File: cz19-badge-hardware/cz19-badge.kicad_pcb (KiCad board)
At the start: 2 copper layers, 128 parts

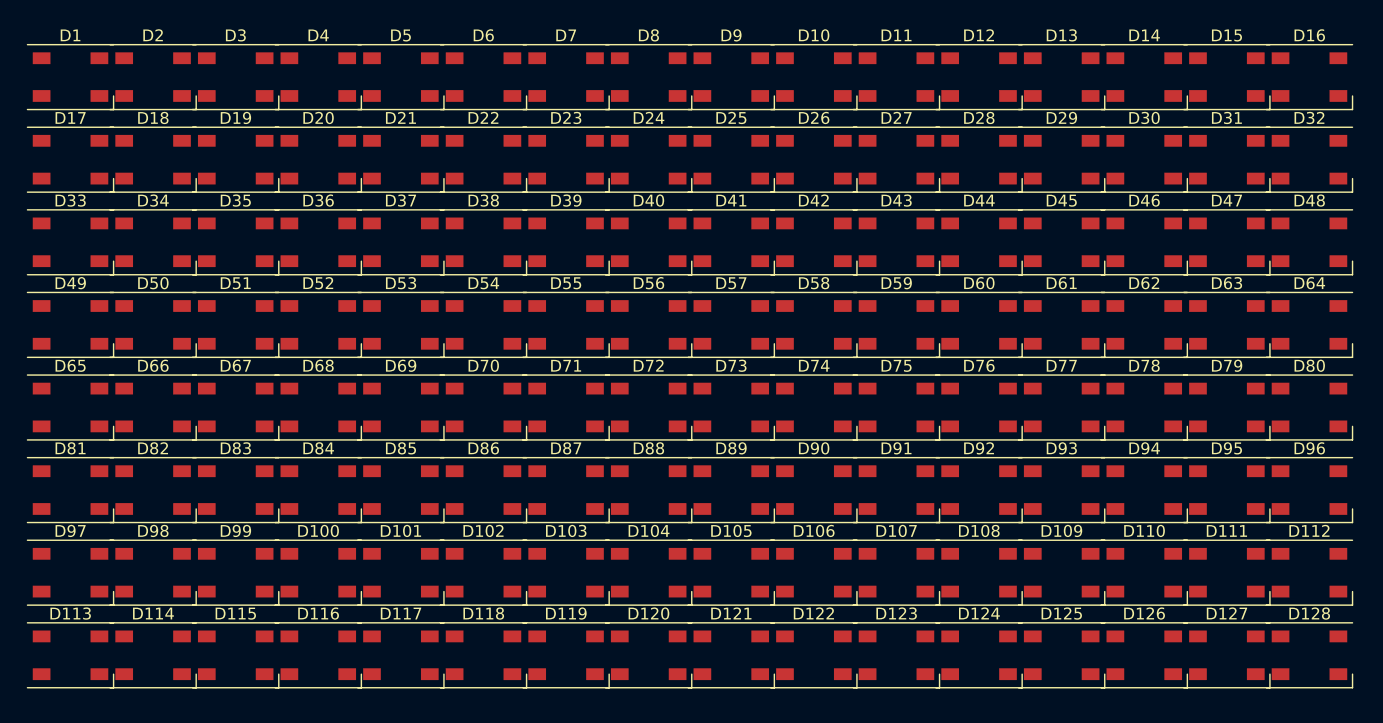
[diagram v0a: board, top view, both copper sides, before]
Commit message: Finished components for USB flashing, and controlling the LEDs w/ mosfet power
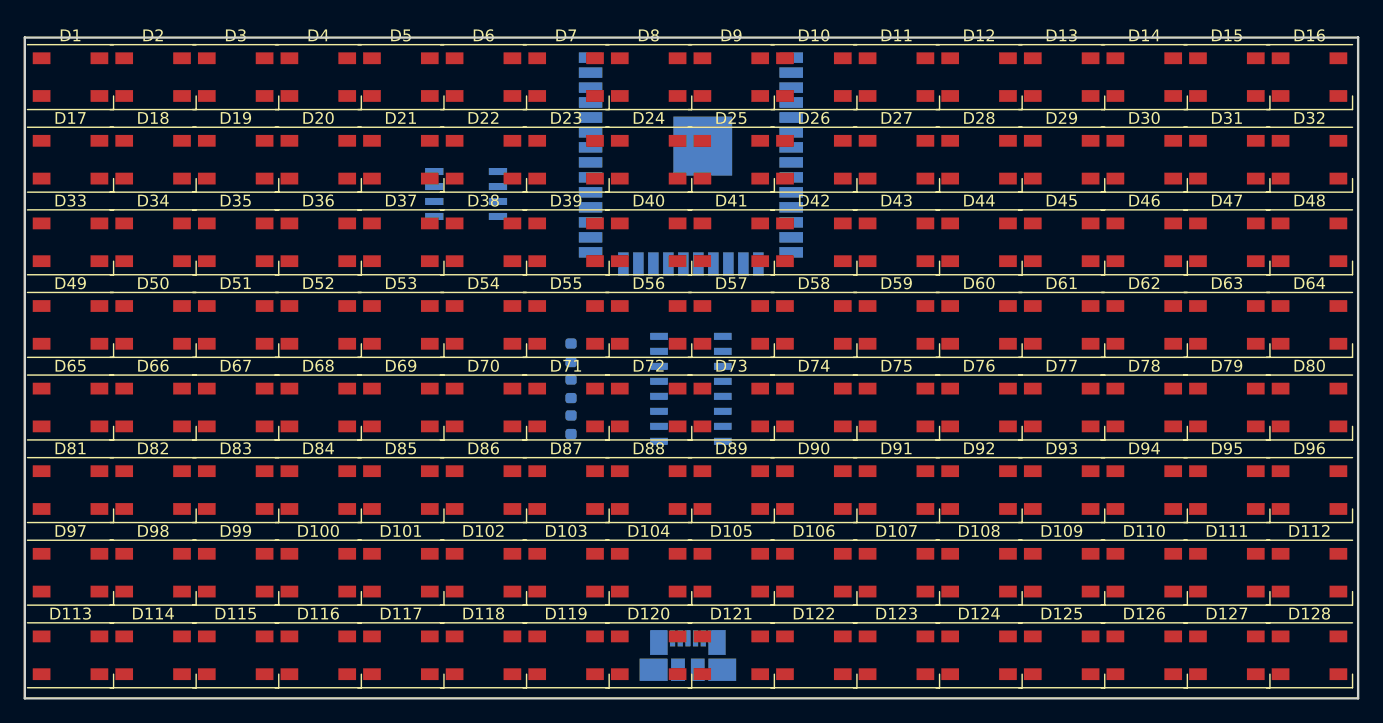
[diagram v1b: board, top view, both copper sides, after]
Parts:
- added J1: USB_B_Micro, Connector_USB:USB_Micro-B_Molex_47346-0001, B.Cu at (76.2, 71.4)
- added Q1: FDS8896, Package_SO:SOIC-8_3.9x4.9mm_P1.27mm, B.Cu at (57.4, 32.3)
- added R1: 10k, Resistor_SMD:R_0603_1608Metric, B.Cu at (66.3, 51.8)
- added R2: 10k, Resistor_SMD:R_0603_1608Metric, B.Cu at (66.3, 48.8)
- added R3: 10k, Resistor_SMD:R_0603_1608Metric, B.Cu at (66.3, 45.7)
- added U1: CH340C, Package_SO:SOIC-16_3.9x9.9mm_P1.27mm, B.Cu at (76.5, 48.8)
- added U2: ESP32-WROOM-32D, RF_Module:ESP32-WROOM-32, B.Cu at (76.5, 28.9)
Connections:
- net /LEDs/LEDS_OUT renamed LEDS_OUT
- net 3V3 renamed VCC
- D1 pad 2: /LEDs/LEDS_IN -> LEDS_IN
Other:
- board outline added: 113 x 56 mm
- copper layers 2 -> 4

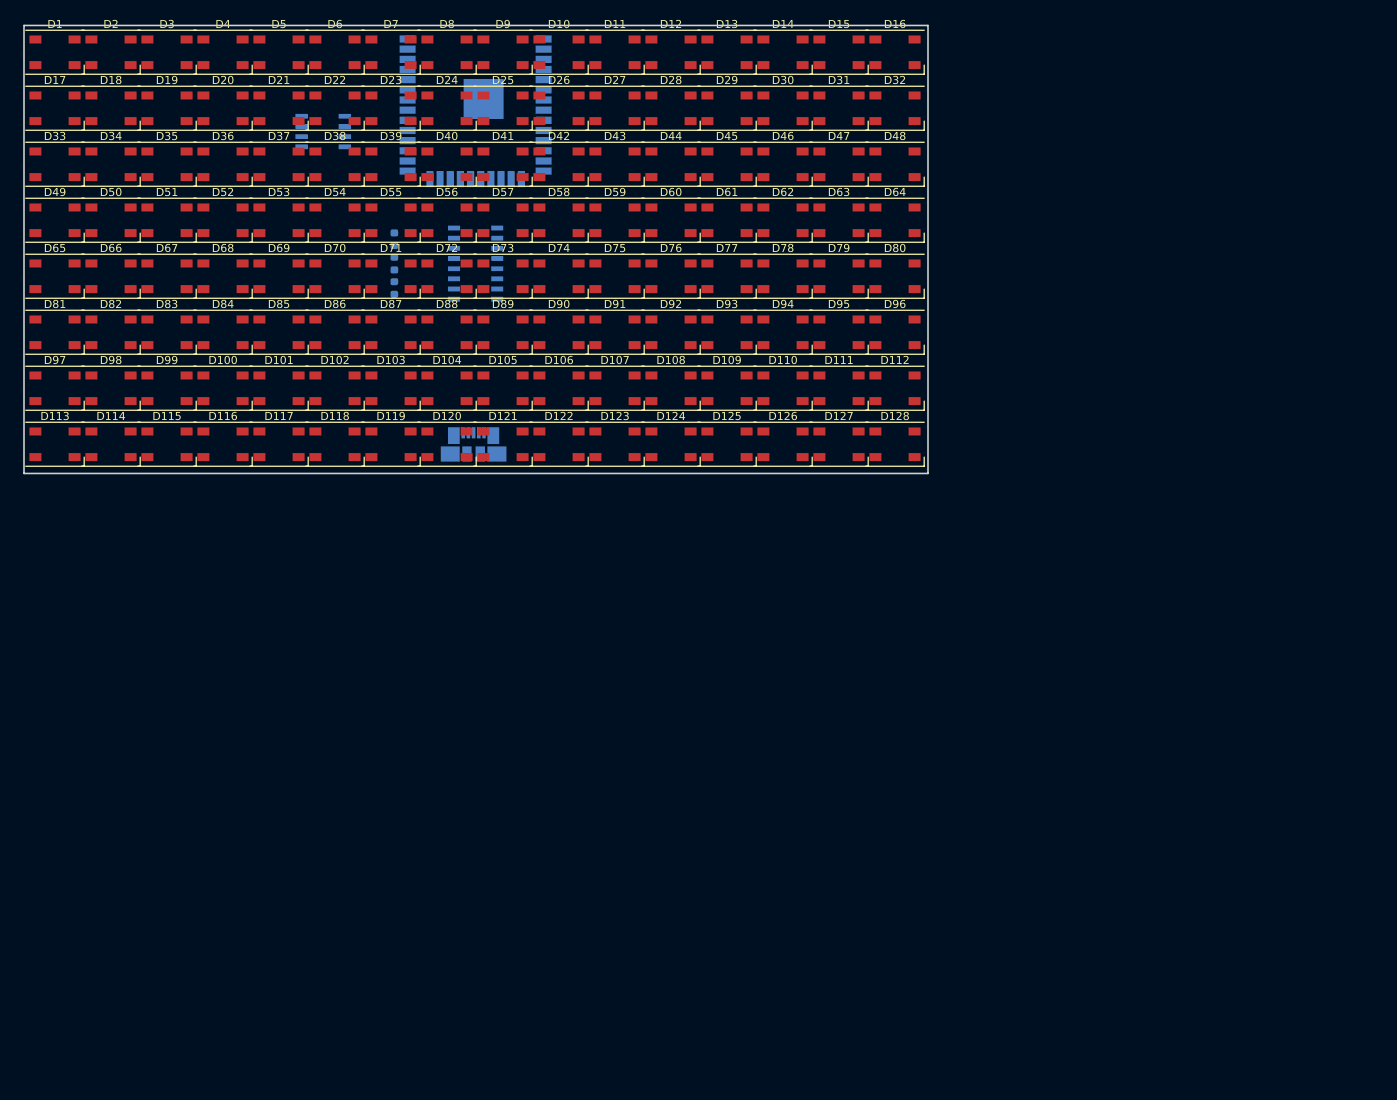
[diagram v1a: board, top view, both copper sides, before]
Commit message: Added extra led columns w/ solder jumper to go back to 8x16, added RTS/DTR fets instead of diodes, added battery circuit w/ reverse polarity protection + automatic switching to USB power
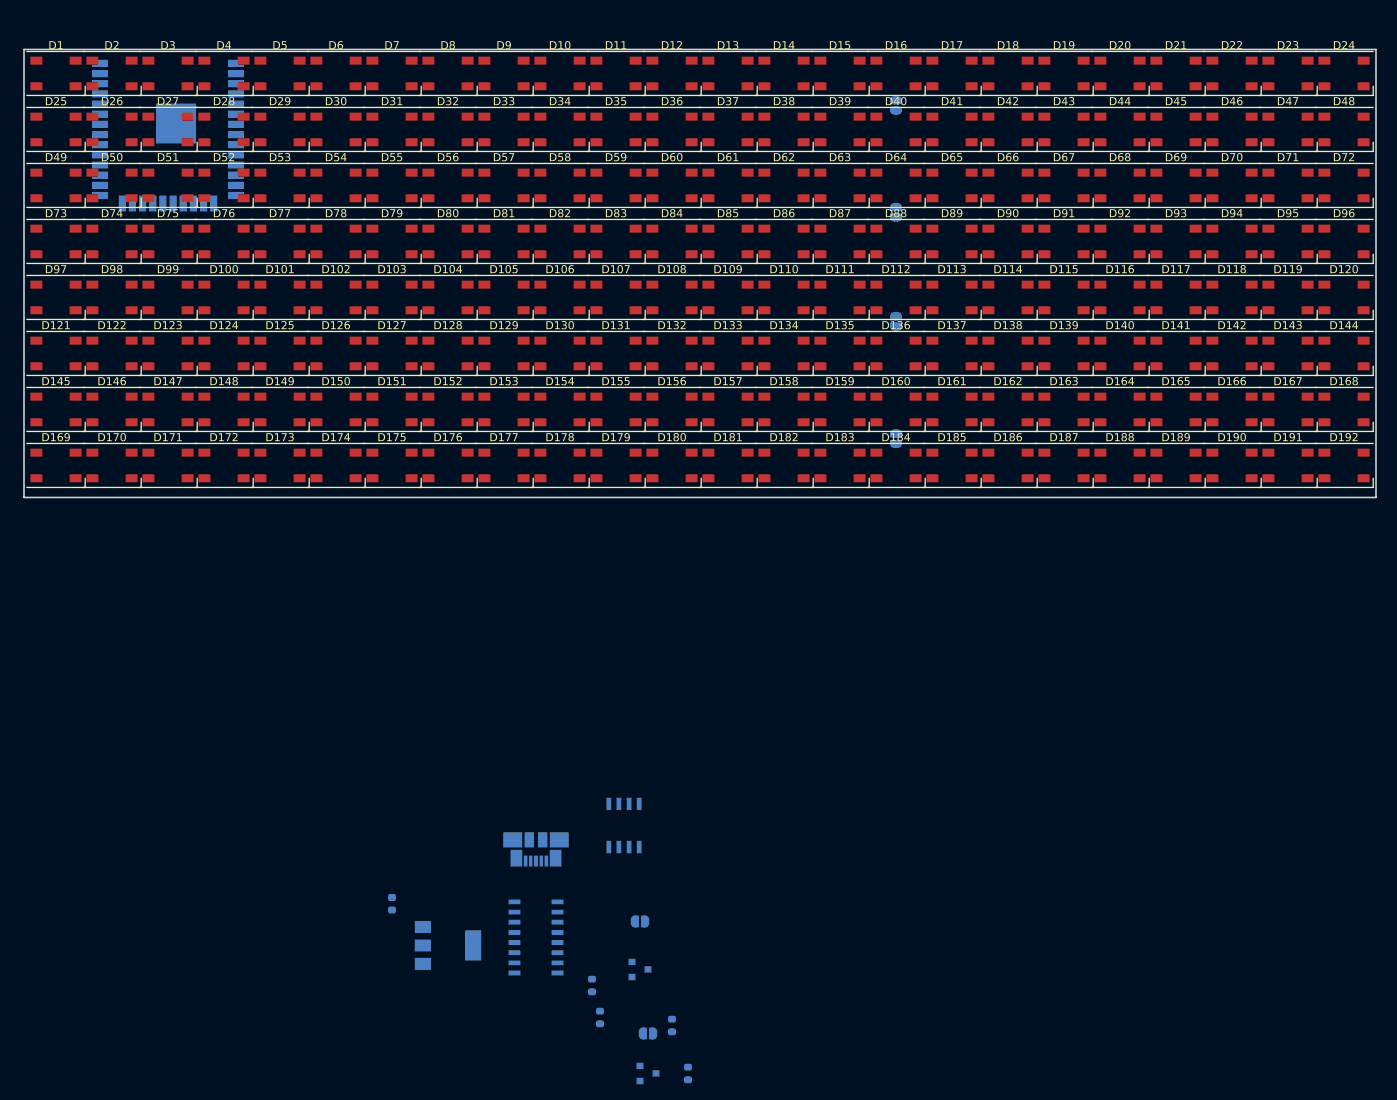
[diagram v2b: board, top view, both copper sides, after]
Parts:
- added D129: SK6812, LED_SMD:LED_SK6812_PLCC4_5.0x5.0mm_P3.2mm, F.Cu at (80.0, 60.0)
- added D130: SK6812, LED_SMD:LED_SK6812_PLCC4_5.0x5.0mm_P3.2mm, F.Cu at (87.0, 60.0)
- added D131: SK6812, LED_SMD:LED_SK6812_PLCC4_5.0x5.0mm_P3.2mm, F.Cu at (94.0, 60.0)
- added D132: SK6812, LED_SMD:LED_SK6812_PLCC4_5.0x5.0mm_P3.2mm, F.Cu at (101.0, 60.0)
- added D133: SK6812, LED_SMD:LED_SK6812_PLCC4_5.0x5.0mm_P3.2mm, F.Cu at (108.0, 60.0)
- added D134: SK6812, LED_SMD:LED_SK6812_PLCC4_5.0x5.0mm_P3.2mm, F.Cu at (115.0, 60.0)
- added D135: SK6812, LED_SMD:LED_SK6812_PLCC4_5.0x5.0mm_P3.2mm, F.Cu at (122.0, 60.0)
- added D136: SK6812, LED_SMD:LED_SK6812_PLCC4_5.0x5.0mm_P3.2mm, F.Cu at (129.0, 60.0)
- added D137: SK6812, LED_SMD:LED_SK6812_PLCC4_5.0x5.0mm_P3.2mm, F.Cu at (136.0, 60.0)
- added D138: SK6812, LED_SMD:LED_SK6812_PLCC4_5.0x5.0mm_P3.2mm, F.Cu at (143.0, 60.0)
- added D139: SK6812, LED_SMD:LED_SK6812_PLCC4_5.0x5.0mm_P3.2mm, F.Cu at (150.0, 60.0)
- added D140: SK6812, LED_SMD:LED_SK6812_PLCC4_5.0x5.0mm_P3.2mm, F.Cu at (157.0, 60.0)
- added D141: SK6812, LED_SMD:LED_SK6812_PLCC4_5.0x5.0mm_P3.2mm, F.Cu at (164.0, 60.0)
- added D142: SK6812, LED_SMD:LED_SK6812_PLCC4_5.0x5.0mm_P3.2mm, F.Cu at (171.0, 60.0)
- added D143: SK6812, LED_SMD:LED_SK6812_PLCC4_5.0x5.0mm_P3.2mm, F.Cu at (178.0, 60.0)
- added D144: SK6812, LED_SMD:LED_SK6812_PLCC4_5.0x5.0mm_P3.2mm, F.Cu at (185.0, 60.0)
- added D145: SK6812, LED_SMD:LED_SK6812_PLCC4_5.0x5.0mm_P3.2mm, F.Cu at (24.0, 67.0)
- added D146: SK6812, LED_SMD:LED_SK6812_PLCC4_5.0x5.0mm_P3.2mm, F.Cu at (31.0, 67.0)
- added D147: SK6812, LED_SMD:LED_SK6812_PLCC4_5.0x5.0mm_P3.2mm, F.Cu at (38.0, 67.0)
- added D148: SK6812, LED_SMD:LED_SK6812_PLCC4_5.0x5.0mm_P3.2mm, F.Cu at (45.0, 67.0)
- added D149: SK6812, LED_SMD:LED_SK6812_PLCC4_5.0x5.0mm_P3.2mm, F.Cu at (52.0, 67.0)
- added D150: SK6812, LED_SMD:LED_SK6812_PLCC4_5.0x5.0mm_P3.2mm, F.Cu at (59.0, 67.0)
- added D151: SK6812, LED_SMD:LED_SK6812_PLCC4_5.0x5.0mm_P3.2mm, F.Cu at (66.0, 67.0)
- added D152: SK6812, LED_SMD:LED_SK6812_PLCC4_5.0x5.0mm_P3.2mm, F.Cu at (73.0, 67.0)
- added D153: SK6812, LED_SMD:LED_SK6812_PLCC4_5.0x5.0mm_P3.2mm, F.Cu at (80.0, 67.0)
- added D154: SK6812, LED_SMD:LED_SK6812_PLCC4_5.0x5.0mm_P3.2mm, F.Cu at (87.0, 67.0)
- added D155: SK6812, LED_SMD:LED_SK6812_PLCC4_5.0x5.0mm_P3.2mm, F.Cu at (94.0, 67.0)
- added D156: SK6812, LED_SMD:LED_SK6812_PLCC4_5.0x5.0mm_P3.2mm, F.Cu at (101.0, 67.0)
- added D157: SK6812, LED_SMD:LED_SK6812_PLCC4_5.0x5.0mm_P3.2mm, F.Cu at (108.0, 67.0)
- added D158: SK6812, LED_SMD:LED_SK6812_PLCC4_5.0x5.0mm_P3.2mm, F.Cu at (115.0, 67.0)
- added D159: SK6812, LED_SMD:LED_SK6812_PLCC4_5.0x5.0mm_P3.2mm, F.Cu at (122.0, 67.0)
- added D160: SK6812, LED_SMD:LED_SK6812_PLCC4_5.0x5.0mm_P3.2mm, F.Cu at (129.0, 67.0)
- added D161: SK6812, LED_SMD:LED_SK6812_PLCC4_5.0x5.0mm_P3.2mm, F.Cu at (136.0, 67.0)
- added D162: SK6812, LED_SMD:LED_SK6812_PLCC4_5.0x5.0mm_P3.2mm, F.Cu at (143.0, 67.0)
- added D163: SK6812, LED_SMD:LED_SK6812_PLCC4_5.0x5.0mm_P3.2mm, F.Cu at (150.0, 67.0)
- added D164: SK6812, LED_SMD:LED_SK6812_PLCC4_5.0x5.0mm_P3.2mm, F.Cu at (157.0, 67.0)
- added D165: SK6812, LED_SMD:LED_SK6812_PLCC4_5.0x5.0mm_P3.2mm, F.Cu at (164.0, 67.0)
- added D166: SK6812, LED_SMD:LED_SK6812_PLCC4_5.0x5.0mm_P3.2mm, F.Cu at (171.0, 67.0)
- added D167: SK6812, LED_SMD:LED_SK6812_PLCC4_5.0x5.0mm_P3.2mm, F.Cu at (178.0, 67.0)
- added D168: SK6812, LED_SMD:LED_SK6812_PLCC4_5.0x5.0mm_P3.2mm, F.Cu at (185.0, 67.0)
- added D169: SK6812, LED_SMD:LED_SK6812_PLCC4_5.0x5.0mm_P3.2mm, F.Cu at (24.0, 74.0)
- added D170: SK6812, LED_SMD:LED_SK6812_PLCC4_5.0x5.0mm_P3.2mm, F.Cu at (31.0, 74.0)
- added D171: SK6812, LED_SMD:LED_SK6812_PLCC4_5.0x5.0mm_P3.2mm, F.Cu at (38.0, 74.0)
- added D172: SK6812, LED_SMD:LED_SK6812_PLCC4_5.0x5.0mm_P3.2mm, F.Cu at (45.0, 74.0)
- added D173: SK6812, LED_SMD:LED_SK6812_PLCC4_5.0x5.0mm_P3.2mm, F.Cu at (52.0, 74.0)
- added D174: SK6812, LED_SMD:LED_SK6812_PLCC4_5.0x5.0mm_P3.2mm, F.Cu at (59.0, 74.0)
- added D175: SK6812, LED_SMD:LED_SK6812_PLCC4_5.0x5.0mm_P3.2mm, F.Cu at (66.0, 74.0)
- added D176: SK6812, LED_SMD:LED_SK6812_PLCC4_5.0x5.0mm_P3.2mm, F.Cu at (73.0, 74.0)
- added D177: SK6812, LED_SMD:LED_SK6812_PLCC4_5.0x5.0mm_P3.2mm, F.Cu at (80.0, 74.0)
- added D178: SK6812, LED_SMD:LED_SK6812_PLCC4_5.0x5.0mm_P3.2mm, F.Cu at (87.0, 74.0)
- added D179: SK6812, LED_SMD:LED_SK6812_PLCC4_5.0x5.0mm_P3.2mm, F.Cu at (94.0, 74.0)
- added D180: SK6812, LED_SMD:LED_SK6812_PLCC4_5.0x5.0mm_P3.2mm, F.Cu at (101.0, 74.0)
- added D181: SK6812, LED_SMD:LED_SK6812_PLCC4_5.0x5.0mm_P3.2mm, F.Cu at (108.0, 74.0)
- added D182: SK6812, LED_SMD:LED_SK6812_PLCC4_5.0x5.0mm_P3.2mm, F.Cu at (115.0, 74.0)
- added D183: SK6812, LED_SMD:LED_SK6812_PLCC4_5.0x5.0mm_P3.2mm, F.Cu at (122.0, 74.0)
- added D184: SK6812, LED_SMD:LED_SK6812_PLCC4_5.0x5.0mm_P3.2mm, F.Cu at (129.0, 74.0)
- added D185: SK6812, LED_SMD:LED_SK6812_PLCC4_5.0x5.0mm_P3.2mm, F.Cu at (136.0, 74.0)
- added D186: SK6812, LED_SMD:LED_SK6812_PLCC4_5.0x5.0mm_P3.2mm, F.Cu at (143.0, 74.0)
- added D187: SK6812, LED_SMD:LED_SK6812_PLCC4_5.0x5.0mm_P3.2mm, F.Cu at (150.0, 74.0)
- added D188: SK6812, LED_SMD:LED_SK6812_PLCC4_5.0x5.0mm_P3.2mm, F.Cu at (157.0, 74.0)
- added D189: SK6812, LED_SMD:LED_SK6812_PLCC4_5.0x5.0mm_P3.2mm, F.Cu at (164.0, 74.0)
- added D190: SK6812, LED_SMD:LED_SK6812_PLCC4_5.0x5.0mm_P3.2mm, F.Cu at (171.0, 74.0)
- added D191: SK6812, LED_SMD:LED_SK6812_PLCC4_5.0x5.0mm_P3.2mm, F.Cu at (178.0, 74.0)
- added D192: SK6812, LED_SMD:LED_SK6812_PLCC4_5.0x5.0mm_P3.2mm, F.Cu at (185.0, 74.0)
- added JP1: SolderJumper_2_Open, Jumper:SolderJumper-2_P1.3mm_Open_RoundedPad1.0x1.5mm, B.Cu at (97.0, 131.0)
- added JP2: SolderJumper_2_Open, Jumper:SolderJumper-2_P1.3mm_Open_RoundedPad1.0x1.5mm, B.Cu at (98.0, 145.0)
- added JP3: SolderJumper_2_Open, Jumper:SolderJumper-2_P1.3mm_Open_RoundedPad1.0x1.5mm, B.Cu at (129.0, 29.0)
- added JP4: SolderJumper_2_Open, Jumper:SolderJumper-2_P1.3mm_Open_RoundedPad1.0x1.5mm, B.Cu at (129.0, 42.4)
- added JP5: SolderJumper_2_Open, Jumper:SolderJumper-2_P1.3mm_Open_RoundedPad1.0x1.5mm, B.Cu at (129.0, 56.0)
- added JP6: SolderJumper_2_Open, Jumper:SolderJumper-2_P1.3mm_Open_RoundedPad1.0x1.5mm, B.Cu at (129.0, 70.7)
- added Q2: MMBT2222A, Package_TO_SOT_SMD:SOT-23, B.Cu at (98.0, 150.0)
- added Q3: FDS8896, Package_SO:SOIC-8_3.9x4.9mm_P1.27mm, B.Cu at (95.0, 119.0)
- added R4: 10k, Resistor_SMD:R_0603_1608Metric, B.Cu at (66.0, 128.8)
- added R5: 10k, Resistor_SMD:R_0603_1608Metric, B.Cu at (103.0, 150.0)
- added U3: AMS1117, Package_TO_SOT_SMD:SOT-223-3_TabPin2, B.Cu at (73.0, 134.0)
- Q1: value FDS8896 -> MMBT2222A; footprint Package_SO:SOIC-8_3.9x4.9mm_P1.27mm -> Package_TO_SOT_SMD:SOT-23
- moved D113 113.6 mm to (136.0, 53.0)
- moved D114 113.6 mm to (143.0, 53.0)
- moved D115 113.6 mm to (150.0, 53.0)
- moved D116 113.6 mm to (157.0, 53.0)
- moved D117 113.6 mm to (164.0, 53.0)
- moved D118 113.6 mm to (171.0, 53.0)
- moved D119 113.6 mm to (178.0, 53.0)
- moved D120 113.6 mm to (185.0, 53.0)
- moved D65 112.7 mm to (136.0, 39.0)
- moved D66 112.7 mm to (143.0, 39.0)
- moved D67 112.7 mm to (150.0, 39.0)
- moved D68 112.7 mm to (157.0, 39.0)
- moved D69 112.7 mm to (164.0, 39.0)
- moved D70 112.7 mm to (171.0, 39.0)
- moved D71 112.7 mm to (178.0, 39.0)
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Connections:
- D1 pad 1: VCC -> 5V_USB
- D10 pad 1: VCC -> 5V_USB
- D100 pad 1: VCC -> 5V_USB
- D101 pad 1: VCC -> 5V_USB
- D102 pad 1: VCC -> 5V_USB
- D103 pad 1: VCC -> 5V_USB
- D104 pad 1: VCC -> 5V_USB
- D105 pad 1: VCC -> 5V_USB
- D106 pad 1: VCC -> 5V_USB
- D107 pad 1: VCC -> 5V_USB
- D108 pad 1: VCC -> 5V_USB
- D109 pad 1: VCC -> 5V_USB
- D11 pad 1: VCC -> 5V_USB
- D110 pad 1: VCC -> 5V_USB
- D111 pad 1: VCC -> 5V_USB
- D112 pad 1: VCC -> 5V_USB
- D113 pad 1: VCC -> 5V_USB
- D113 pad 2: Net-(D113-Pad2) -> Net-(D112-Pad4)
- D113 pad 4: LEDS_OUT -> Net-(D113-Pad4)
- D114 pad 1: VCC -> 5V_USB
- D114 pad 2: Net-(D114-Pad2) -> Net-(D113-Pad4)
- D114 pad 4: Net-(D113-Pad2) -> Net-(D114-Pad4)
- D115 pad 1: VCC -> 5V_USB
- D115 pad 2: Net-(D115-Pad2) -> Net-(D114-Pad4)
- D115 pad 4: Net-(D114-Pad2) -> Net-(D115-Pad4)
- D116 pad 1: VCC -> 5V_USB
- D116 pad 2: Net-(D116-Pad2) -> Net-(D115-Pad4)
- D116 pad 4: Net-(D115-Pad2) -> Net-(D116-Pad4)
- D117 pad 1: VCC -> 5V_USB
- D117 pad 2: Net-(D117-Pad2) -> Net-(D116-Pad4)
- D117 pad 4: Net-(D116-Pad2) -> Net-(D117-Pad4)
- D118 pad 1: VCC -> 5V_USB
- D118 pad 2: Net-(D118-Pad2) -> Net-(D117-Pad4)
- D118 pad 4: Net-(D117-Pad2) -> Net-(D118-Pad4)
- D119 pad 1: VCC -> 5V_USB
- D119 pad 2: Net-(D119-Pad2) -> Net-(D118-Pad4)
- D119 pad 4: Net-(D118-Pad2) -> Net-(D119-Pad4)
- D12 pad 1: VCC -> 5V_USB
- D120 pad 1: VCC -> 5V_USB
- D120 pad 2: Net-(D120-Pad2) -> Net-(D119-Pad4)
- D120 pad 4: Net-(D119-Pad2) -> Net-(D120-Pad4)
- D121 pad 1: VCC -> 5V_USB
- D121 pad 4: Net-(D120-Pad2) -> Net-(D121-Pad4)
- D122 pad 1: VCC -> 5V_USB
- D123 pad 1: VCC -> 5V_USB
- D124 pad 1: VCC -> 5V_USB
- D125 pad 1: VCC -> 5V_USB
- D126 pad 1: VCC -> 5V_USB
- D127 pad 1: VCC -> 5V_USB
- D128 pad 1: VCC -> 5V_USB
- D128 pad 2: Net-(D112-Pad4) -> Net-(D128-Pad2)
- D13 pad 1: VCC -> 5V_USB
- D14 pad 1: VCC -> 5V_USB
- D15 pad 1: VCC -> 5V_USB
- D16 pad 1: VCC -> 5V_USB
- D17 pad 1: VCC -> 5V_USB
- D17 pad 2: Net-(D17-Pad2) -> Net-(D16-Pad4)
- D18 pad 1: VCC -> 5V_USB
- D18 pad 2: Net-(D18-Pad2) -> Net-(D17-Pad4)
- D18 pad 4: Net-(D17-Pad2) -> Net-(D18-Pad4)
- D19 pad 1: VCC -> 5V_USB
- D19 pad 2: Net-(D19-Pad2) -> Net-(D18-Pad4)
- D19 pad 4: Net-(D18-Pad2) -> Net-(D19-Pad4)
- D2 pad 1: VCC -> 5V_USB
- D20 pad 1: VCC -> 5V_USB
- D20 pad 2: Net-(D20-Pad2) -> Net-(D19-Pad4)
- D20 pad 4: Net-(D19-Pad2) -> Net-(D20-Pad4)
- D21 pad 1: VCC -> 5V_USB
- D21 pad 2: Net-(D21-Pad2) -> Net-(D20-Pad4)
- D21 pad 4: Net-(D20-Pad2) -> Net-(D21-Pad4)
- D22 pad 1: VCC -> 5V_USB
- D22 pad 2: Net-(D22-Pad2) -> Net-(D21-Pad4)
- D22 pad 4: Net-(D21-Pad2) -> Net-(D22-Pad4)
- D23 pad 1: VCC -> 5V_USB
- D23 pad 2: Net-(D23-Pad2) -> Net-(D22-Pad4)
- D23 pad 4: Net-(D22-Pad2) -> Net-(D23-Pad4)
- D24 pad 1: VCC -> 5V_USB
- D24 pad 2: Net-(D24-Pad2) -> Net-(D23-Pad4)
- D24 pad 4: Net-(D23-Pad2) -> Net-(D24-Pad4)
- D25 pad 1: VCC -> 5V_USB
- D25 pad 4: Net-(D24-Pad2) -> Net-(D25-Pad4)
- D26 pad 1: VCC -> 5V_USB
- D27 pad 1: VCC -> 5V_USB
- D28 pad 1: VCC -> 5V_USB
- D29 pad 1: VCC -> 5V_USB
- D3 pad 1: VCC -> 5V_USB
- D30 pad 1: VCC -> 5V_USB
- D31 pad 1: VCC -> 5V_USB
- D32 pad 1: VCC -> 5V_USB
- D32 pad 2: Net-(D16-Pad4) -> Net-(D32-Pad2)
- D33 pad 1: VCC -> 5V_USB
- D33 pad 2: Net-(D17-Pad4) -> Net-(D33-Pad2)
- D33 pad 4: Net-(D33-Pad4) -> Net-(D32-Pad2)
- D34 pad 1: VCC -> 5V_USB
- D34 pad 2: Net-(D33-Pad4) -> Net-(D34-Pad2)
- D34 pad 4: Net-(D34-Pad4) -> Net-(D33-Pad2)
- D35 pad 1: VCC -> 5V_USB
- D35 pad 2: Net-(D34-Pad4) -> Net-(D35-Pad2)
- D35 pad 4: Net-(D35-Pad4) -> Net-(D34-Pad2)
- D36 pad 1: VCC -> 5V_USB
- D36 pad 2: Net-(D35-Pad4) -> Net-(D36-Pad2)
- D36 pad 4: Net-(D36-Pad4) -> Net-(D35-Pad2)
- D37 pad 1: VCC -> 5V_USB
- D37 pad 2: Net-(D36-Pad4) -> Net-(D37-Pad2)
- D37 pad 4: Net-(D37-Pad4) -> Net-(D36-Pad2)
- D38 pad 1: VCC -> 5V_USB
- D38 pad 2: Net-(D37-Pad4) -> Net-(D38-Pad2)
- D38 pad 4: Net-(D38-Pad4) -> Net-(D37-Pad2)
- D39 pad 1: VCC -> 5V_USB
- D39 pad 2: Net-(D38-Pad4) -> Net-(D39-Pad2)
- D39 pad 4: Net-(D39-Pad4) -> Net-(D38-Pad2)
- D4 pad 1: VCC -> 5V_USB
- D40 pad 1: VCC -> 5V_USB
- D40 pad 2: Net-(D39-Pad4) -> Net-(D40-Pad2)
- D40 pad 4: Net-(D40-Pad4) -> Net-(D39-Pad2)
- D41 pad 1: VCC -> 5V_USB
- D41 pad 2: Net-(D40-Pad4) -> Net-(D41-Pad2)
- D41 pad 4: Net-(D41-Pad4) -> Net-(D40-Pad2)
- D42 pad 1: VCC -> 5V_USB
- D42 pad 2: Net-(D41-Pad4) -> Net-(D42-Pad2)
- D42 pad 4: Net-(D42-Pad4) -> Net-(D41-Pad2)
- D43 pad 1: VCC -> 5V_USB
- D43 pad 2: Net-(D42-Pad4) -> Net-(D43-Pad2)
- D43 pad 4: Net-(D43-Pad4) -> Net-(D42-Pad2)
- D44 pad 1: VCC -> 5V_USB
- D44 pad 2: Net-(D43-Pad4) -> Net-(D44-Pad2)
- D44 pad 4: Net-(D44-Pad4) -> Net-(D43-Pad2)
- D45 pad 1: VCC -> 5V_USB
- D45 pad 2: Net-(D44-Pad4) -> Net-(D45-Pad2)
- D45 pad 4: Net-(D45-Pad4) -> Net-(D44-Pad2)
- D46 pad 1: VCC -> 5V_USB
- D46 pad 2: Net-(D45-Pad4) -> Net-(D46-Pad2)
- D46 pad 4: Net-(D46-Pad4) -> Net-(D45-Pad2)
- D47 pad 1: VCC -> 5V_USB
- D47 pad 2: Net-(D46-Pad4) -> Net-(D47-Pad2)
- D47 pad 4: Net-(D47-Pad4) -> Net-(D46-Pad2)
- D48 pad 1: VCC -> 5V_USB
- D48 pad 2: Net-(D47-Pad4) -> Net-(D24-Pad4)
- D48 pad 4: Net-(D48-Pad4) -> Net-(D47-Pad2)
- D49 pad 1: VCC -> 5V_USB
- D49 pad 2: Net-(D49-Pad2) -> Net-(D25-Pad4)
- D5 pad 1: VCC -> 5V_USB
- D50 pad 1: VCC -> 5V_USB
- D50 pad 2: Net-(D50-Pad2) -> Net-(D49-Pad4)
- D50 pad 4: Net-(D49-Pad2) -> Net-(D50-Pad4)
- D51 pad 1: VCC -> 5V_USB
- D51 pad 2: Net-(D51-Pad2) -> Net-(D50-Pad4)
- D51 pad 4: Net-(D50-Pad2) -> Net-(D51-Pad4)
- D52 pad 1: VCC -> 5V_USB
- D52 pad 2: Net-(D52-Pad2) -> Net-(D51-Pad4)
- D52 pad 4: Net-(D51-Pad2) -> Net-(D52-Pad4)
- D53 pad 1: VCC -> 5V_USB
- D53 pad 2: Net-(D53-Pad2) -> Net-(D52-Pad4)
- D53 pad 4: Net-(D52-Pad2) -> Net-(D53-Pad4)
- D54 pad 1: VCC -> 5V_USB
- D54 pad 2: Net-(D54-Pad2) -> Net-(D53-Pad4)
- D54 pad 4: Net-(D53-Pad2) -> Net-(D54-Pad4)
- D55 pad 1: VCC -> 5V_USB
- D55 pad 2: Net-(D55-Pad2) -> Net-(D54-Pad4)
- D55 pad 4: Net-(D54-Pad2) -> Net-(D55-Pad4)
- D56 pad 1: VCC -> 5V_USB
- D56 pad 2: Net-(D56-Pad2) -> Net-(D55-Pad4)
- D56 pad 4: Net-(D55-Pad2) -> Net-(D56-Pad4)
- D57 pad 1: VCC -> 5V_USB
- D57 pad 2: Net-(D57-Pad2) -> Net-(D56-Pad4)
- D57 pad 4: Net-(D56-Pad2) -> Net-(D57-Pad4)
- D58 pad 1: VCC -> 5V_USB
- D58 pad 2: Net-(D58-Pad2) -> Net-(D57-Pad4)
- D58 pad 4: Net-(D57-Pad2) -> Net-(D58-Pad4)
- D59 pad 1: VCC -> 5V_USB
- D59 pad 2: Net-(D59-Pad2) -> Net-(D58-Pad4)
- D59 pad 4: Net-(D58-Pad2) -> Net-(D59-Pad4)
- D6 pad 1: VCC -> 5V_USB
- D60 pad 1: VCC -> 5V_USB
- D60 pad 2: Net-(D60-Pad2) -> Net-(D59-Pad4)
- D60 pad 4: Net-(D59-Pad2) -> Net-(D60-Pad4)
- D61 pad 1: VCC -> 5V_USB
- D61 pad 2: Net-(D61-Pad2) -> Net-(D60-Pad4)
- D61 pad 4: Net-(D60-Pad2) -> Net-(D61-Pad4)
- D62 pad 1: VCC -> 5V_USB
- D62 pad 2: Net-(D62-Pad2) -> Net-(D61-Pad4)
- D62 pad 4: Net-(D61-Pad2) -> Net-(D62-Pad4)
- D63 pad 1: VCC -> 5V_USB
- D63 pad 2: Net-(D63-Pad2) -> Net-(D62-Pad4)
- D63 pad 4: Net-(D62-Pad2) -> Net-(D63-Pad4)
- D64 pad 1: VCC -> 5V_USB
- D64 pad 2: Net-(D48-Pad4) -> Net-(D63-Pad4)
- D64 pad 4: Net-(D63-Pad2) -> Net-(D64-Pad4)
- D65 pad 1: VCC -> 5V_USB
- D65 pad 2: Net-(D49-Pad4) -> Net-(D64-Pad4)
- D66 pad 1: VCC -> 5V_USB
- D67 pad 1: VCC -> 5V_USB
- D68 pad 1: VCC -> 5V_USB
- D69 pad 1: VCC -> 5V_USB
- D7 pad 1: VCC -> 5V_USB
- D70 pad 1: VCC -> 5V_USB
- D71 pad 1: VCC -> 5V_USB
- D72 pad 1: VCC -> 5V_USB
- D73 pad 1: VCC -> 5V_USB
- D73 pad 2: Net-(D72-Pad4) -> Net-(D73-Pad2)
- D74 pad 1: VCC -> 5V_USB
- D74 pad 2: Net-(D73-Pad4) -> Net-(D74-Pad2)
- D74 pad 4: Net-(D74-Pad4) -> Net-(D73-Pad2)
- D75 pad 1: VCC -> 5V_USB
- D75 pad 2: Net-(D74-Pad4) -> Net-(D75-Pad2)
- D75 pad 4: Net-(D75-Pad4) -> Net-(D74-Pad2)
- D76 pad 1: VCC -> 5V_USB
- D76 pad 2: Net-(D75-Pad4) -> Net-(D76-Pad2)
- D76 pad 4: Net-(D76-Pad4) -> Net-(D75-Pad2)
- D77 pad 1: VCC -> 5V_USB
- D77 pad 2: Net-(D76-Pad4) -> Net-(D77-Pad2)
- D77 pad 4: Net-(D77-Pad4) -> Net-(D76-Pad2)
- D78 pad 1: VCC -> 5V_USB
- D78 pad 2: Net-(D77-Pad4) -> Net-(D78-Pad2)
- D78 pad 4: Net-(D78-Pad4) -> Net-(D77-Pad2)
- D79 pad 1: VCC -> 5V_USB
- D79 pad 2: Net-(D78-Pad4) -> Net-(D79-Pad2)
- D79 pad 4: Net-(D79-Pad4) -> Net-(D78-Pad2)
- D8 pad 1: VCC -> 5V_USB
- D80 pad 1: VCC -> 5V_USB
- D80 pad 2: Net-(D79-Pad4) -> Net-(D80-Pad2)
- D80 pad 4: Net-(D80-Pad4) -> Net-(D79-Pad2)
- D81 pad 1: VCC -> 5V_USB
- D81 pad 4: Net-(D81-Pad4) -> Net-(D80-Pad2)
- D82 pad 1: VCC -> 5V_USB
- D83 pad 1: VCC -> 5V_USB
- D84 pad 1: VCC -> 5V_USB
- D85 pad 1: VCC -> 5V_USB
- D86 pad 1: VCC -> 5V_USB
- D87 pad 1: VCC -> 5V_USB
- D88 pad 1: VCC -> 5V_USB
- D89 pad 1: VCC -> 5V_USB
- D9 pad 1: VCC -> 5V_USB
- D90 pad 1: VCC -> 5V_USB
- D91 pad 1: VCC -> 5V_USB
- D92 pad 1: VCC -> 5V_USB
- D93 pad 1: VCC -> 5V_USB
- D94 pad 1: VCC -> 5V_USB
- D95 pad 1: VCC -> 5V_USB
- D96 pad 1: VCC -> 5V_USB
- D96 pad 2: Net-(D80-Pad4) -> Net-(D72-Pad4)
- D97 pad 1: VCC -> 5V_USB
- D97 pad 2: Net-(D81-Pad4) -> Net-(D73-Pad4)
- D98 pad 1: VCC -> 5V_USB
- D99 pad 1: VCC -> 5V_USB
- Q1 pad 1: GND -> Net-(Q1-Pad1)
- Q1 pad 2: GND -> ESP_FLASH
- Q1 pad 3: GND -> Net-(JP1-Pad2)
- R1 pad 1: ESP_EN -> Net-(JP2-Pad2)
- R1 pad 2: 3V3 -> Net-(Q1-Pad1)
- R2 pad 1: 3V3 -> ESP_EN
- R2 pad 2: ESP_FLASH -> 3V3
- R3 pad 1: GND -> 3V3
- R3 pad 2: Net-(R3-Pad2) -> ESP_FLASH
- U1 pad 13: ESP_FLASH -> Net-(JP1-Pad2)
- U1 pad 14: ESP_EN -> Net-(JP2-Pad2)
- U2 pad 24: Net-(R3-Pad2) -> Net-(R4-Pad2)
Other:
- board size 113 x 56 mm -> 169 x 56 mm
